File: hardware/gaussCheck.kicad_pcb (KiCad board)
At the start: 2 copper layers, 31.5 x 95.4 mm, 57 parts, among them J1 USB_C_Receptacle_USB2.0, J2 SWD, Q1 BSS138, Q2 BSS83P, SW1 PTS810, SW2 PT847S, SW3 PT847S, SW4 PT847S, U1 TLV493D, U2 VIM-878-DP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

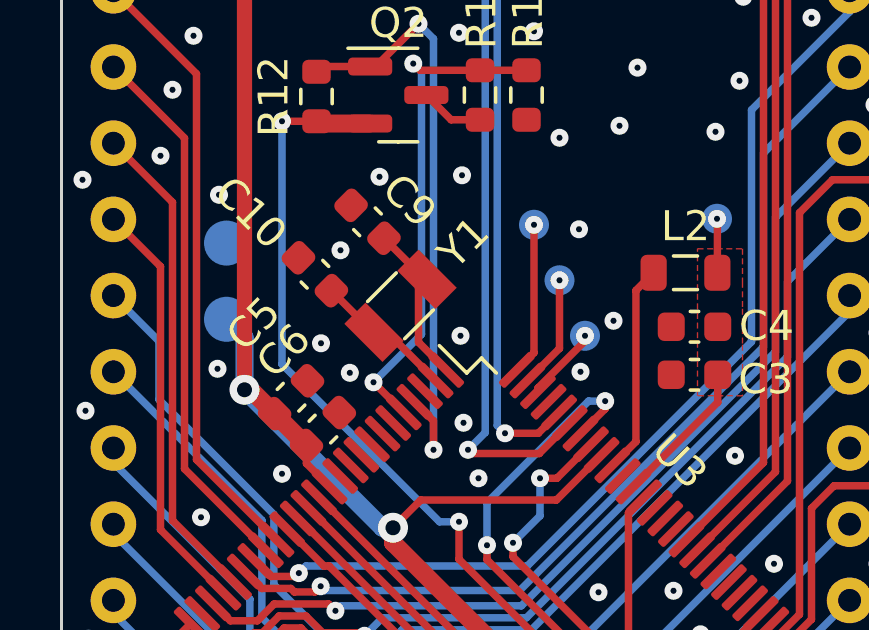
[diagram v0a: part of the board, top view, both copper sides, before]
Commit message: updated some MPNs
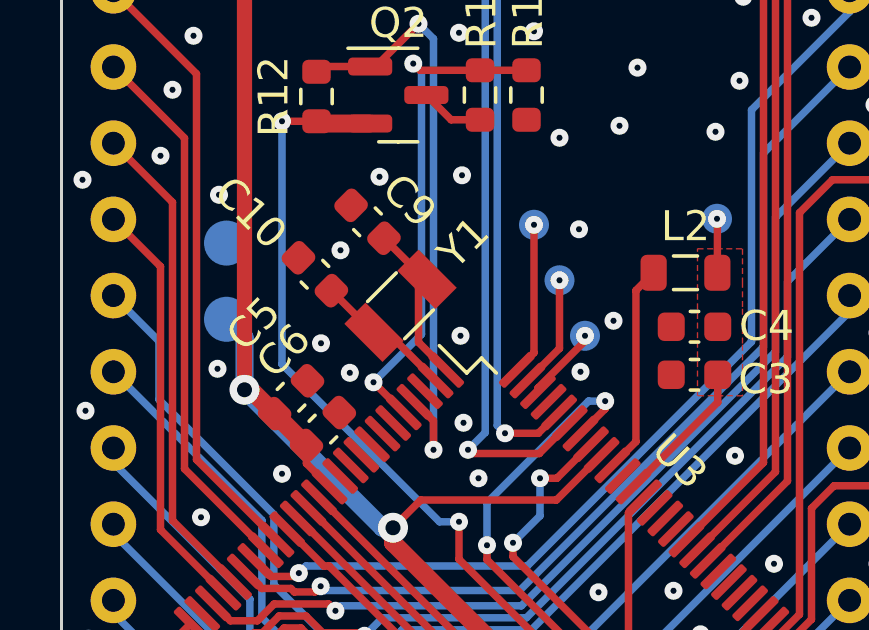
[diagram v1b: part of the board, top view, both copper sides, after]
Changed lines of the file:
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@@
   (segment (start 101.95 84.35) (end 101.95 85.6) (width 0.25) (layer "B.Cu") (net 46))
   (segment (start 105.324606 94.374606) (end 107.65 96.7) (width 0.25) (layer "B.Cu") (net 46))
-  (segment (start 97.9 79.232234) (end 97.9 78) (width 0.25) (layer "F.Cu") (net 47))
+  (segment (start 98.116117 77.716117) (end 96.748008 76.348008) (width 0.25) (layer "F.Cu") (net 47))
   (segment (start 98.824435 80.739154) (end 97.9 79.814719) (width 0.25) (layer "F.Cu") (net 47))
   (segment (start 98.183883 77.716117) (end 98.116117 77.716117) (width 0.25) (layer "F.Cu") (net 47))
-  (segment (start 97.9 79.814719) (end 97.9 79.3) (width 0.25) (layer "F.Cu") (net 47))
-  (segment (start 98.116117 77.716117) (end 96.748008 76.348008) (width 0.25) (layer "F.Cu") (net 47))
+  (segment (start 97.9 79.814719) (end 97.9 78) (width 0.25) (layer "F.Cu") (net 47))
   (segment (start 97.9 78) (end 98.183883 77.716117) (width 0.25) (layer "F.Cu") (net 47))
   (segment (start 96.862058 79.483883) (end 96.416117 79.483883) (width 0.25) (layer "F.Cu") (net 48))

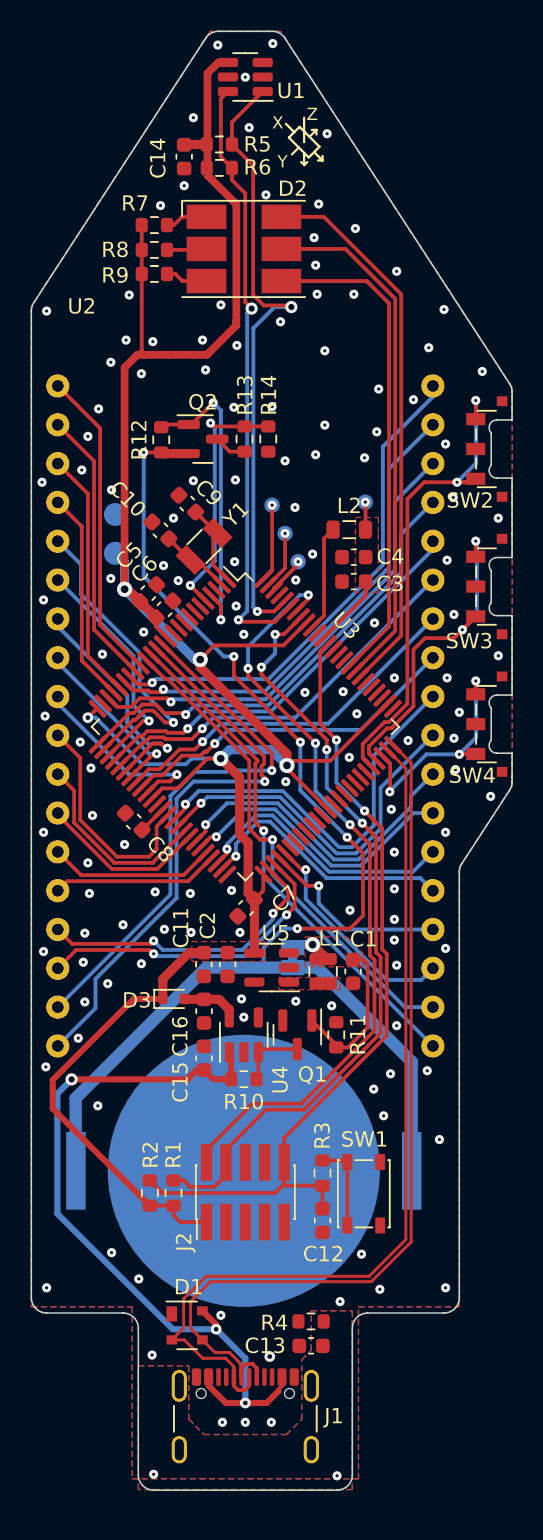
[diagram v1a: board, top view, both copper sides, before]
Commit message: added daughter board for LCD lightning
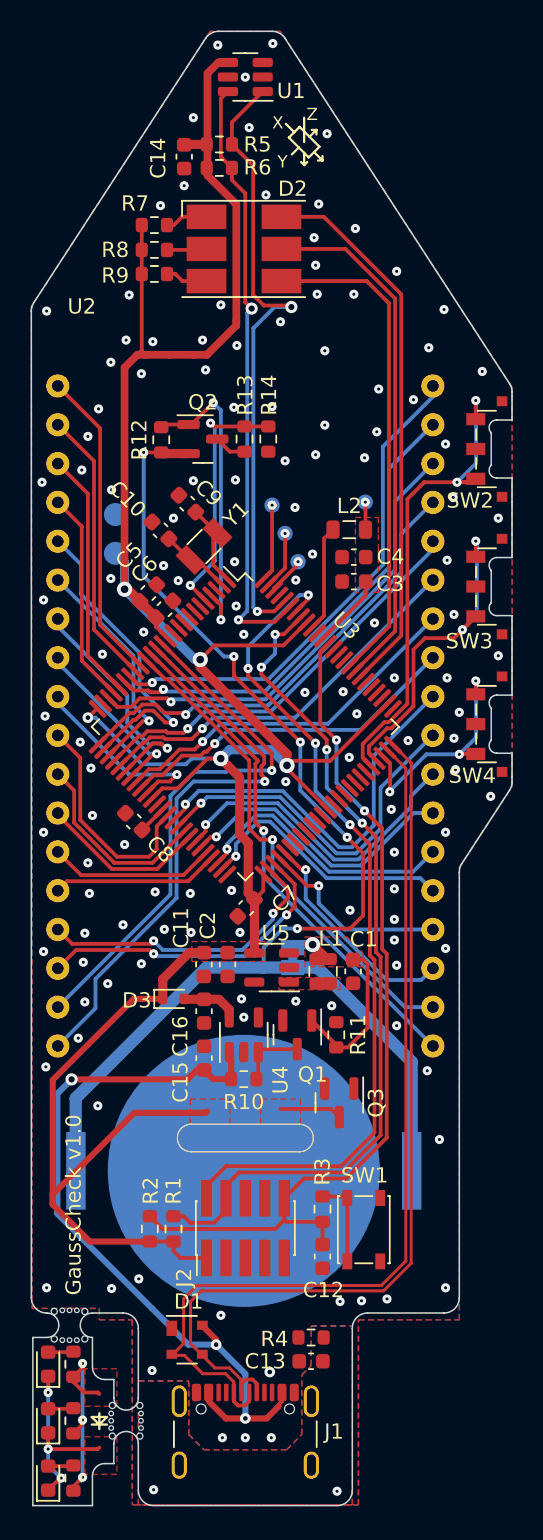
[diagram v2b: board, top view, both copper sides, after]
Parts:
- added D4: LED, LED_SMD:LED_0603_1608Metric, F.Cu at (87.1, 139.6)
- added D5: LED, LED_SMD:LED_0603_1608Metric, F.Cu at (87.1, 135.8)
- added D6: LED, LED_SMD:LED_0603_1608Metric, F.Cu at (87.1, 132.1)
- added Q3: BSS138, Package_TO_SOT_SMD:SOT-23, F.Cu at (106.2, 115.0)
- added R15: 140, Resistor_SMD:R_0603_1608Metric, F.Cu at (88.8, 139.6)
- added R16: 140, Resistor_SMD:R_0603_1608Metric, F.Cu at (88.8, 135.8)
- added R17: 140, Resistor_SMD:R_0603_1608Metric, F.Cu at (88.8, 132.1)
- added REF**: MouseBite_Mill1.6mm, GaussCheckCustomFootprint:MouseBite_Mill1.6mm, F.Cu at (92.2, 135.8)
- added REF**: MouseBite_Mill1.6mm, GaussCheckCustomFootprint:MouseBite_Mill1.6mm, F.Cu at (88.5, 129.6)
- C10, C9: value ??p -> 8p
- moved J2 2.35 mm to (100.0, 123.2)
- moved R3 2.35 mm to (105.0, 122.0)
- moved C12 2.35 mm to (105.0, 125.0)
- moved R1 2.35 mm to (95.3, 123.2)
- moved R2 2.35 mm to (93.8, 123.2)
- moved SW1 2.35 mm to (107.8, 123.3)
- moved R4 1.05 mm to (104.3, 130.3)
- moved C13 1.01 mm to (104.3, 131.9)
- moved J1 1.01 mm to (100.0, 137.6)
- moved D1 0.94 mm to (96.2, 130.5)
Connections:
- U3 pad 61: unconnected-(U3C-PC21/SLCD[41]-Pad61) -> /DisplayLightning/EN_DisplayLED
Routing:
- net +3V3: track 162.0 -> 179.7 mm
- net /DisplayLightning/LED_A: track 0.00 -> 13.2 mm, vias 0 -> 3
- net /DisplayLightning/LED_K: track 0.00 -> 12.6 mm, vias 0 -> 3
- net /MCU/SWDIO: track 50.4 -> 55.3 mm
- net /MCU/SWCLK: track 50.7 -> 55.6 mm
- net /DisplayLightning/D_LED_K: track 0.00 -> 4.07 mm
- net /MCU/~{RESET}: track 53.6 -> 57.5 mm
- net /MCU/D-: track 59.6 -> 61.4 mm
- net /MCU/D+: track 58.4 -> 60.2 mm
- net Net-(D6-A): track 0.00 -> 1.67 mm
- net Net-(D5-A): track 0.00 -> 1.67 mm
- net Net-(D4-A): track 0.00 -> 1.67 mm
- net GND: vias 135 -> 132
- added copper zone on F.Cu, net /DisplayLightning/D_LED_K
- added copper zone on F.Cu, net /DisplayLightning/LED_A
- added copper zone on F.Cu, net /DisplayLightning/LED_K
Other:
- board size 31.5 x 95.4 mm -> 31.5 x 96.4 mm
- board text added: "GaussCheck v1.0"

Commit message: custom LED daughter board for display lightning added resistors to USB-C CC line
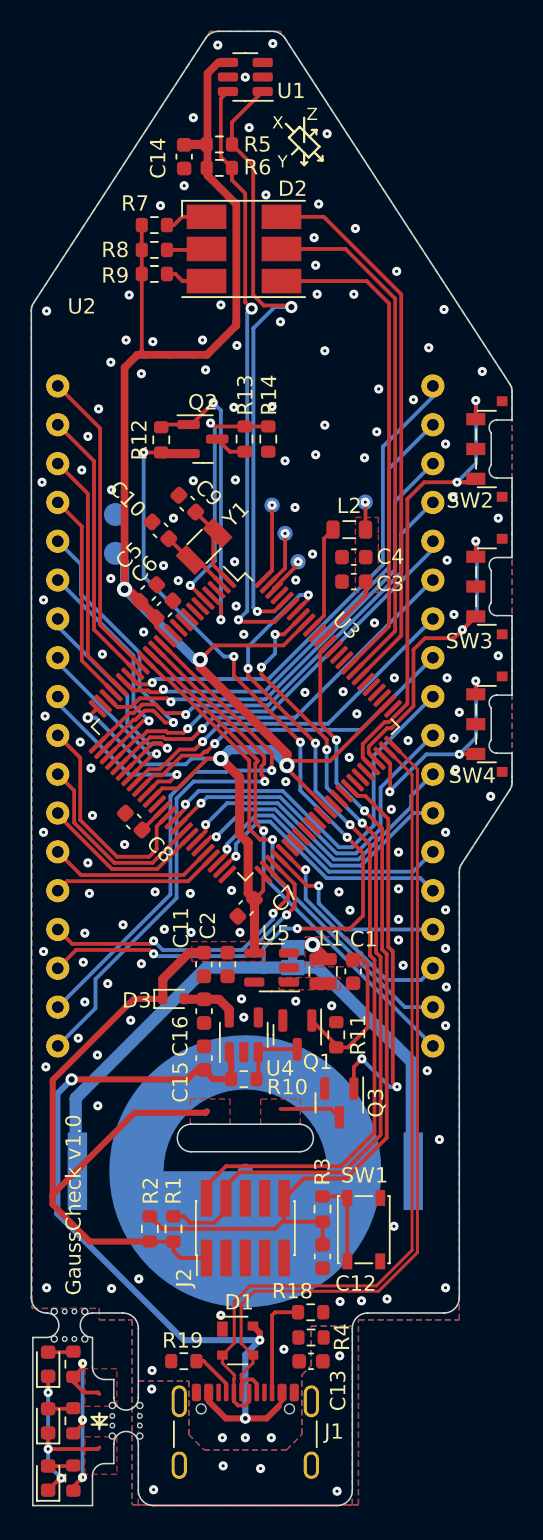
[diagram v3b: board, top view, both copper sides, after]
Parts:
- added R18: 56k, Resistor_SMD:R_0603_1608Metric, F.Cu at (104.3, 128.7)
- added R19: 56k, Resistor_SMD:R_0603_1608Metric, F.Cu at (96.0, 131.9)
- BT1: footprint Battery:BatteryHolder_Keystone_3034_1x20mm -> GaussCheckCustomFootprint:BatteryHolder_Keystone_3034_1x20mm_donut
- moved D1 3.31 mm to (99.5, 130.6)
- moved BT1 0.10 mm to (100.0, 119.5)
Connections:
- J1 pad A5: unconnected-(J1-CC1-PadA5) -> Net-(J1-CC1)
- J1 pad B5: unconnected-(J1-CC2-PadB5) -> Net-(J1-CC2)
- U3 pad 61: /DisplayLightning/EN_DisplayLED -> unconnected-(U3C-PC21/SLCD[41]-Pad61)
- U3 pad 67: unconnected-(U3B-PB19/SLCD[45]-Pad67) -> /DisplayLightning/EN_DisplayLED
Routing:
- net /DisplayLightning/EN_DisplayLED: track 0.00 -> 26.3 mm, vias 0 -> 2
- net Net-(J1-CC2): track 0.00 -> 6.83 mm
- net /MCU/D-: track 61.4 -> 55.4 mm
- net /MCU/D+: track 60.2 -> 55.6 mm
- net Net-(J1-CC1): track 0.00 -> 3.14 mm
- net VBUS: track 49.4 -> 51.6 mm
- net Net-(J1-SHIELD): vias 2 -> 6
- net GND: vias 132 -> 138

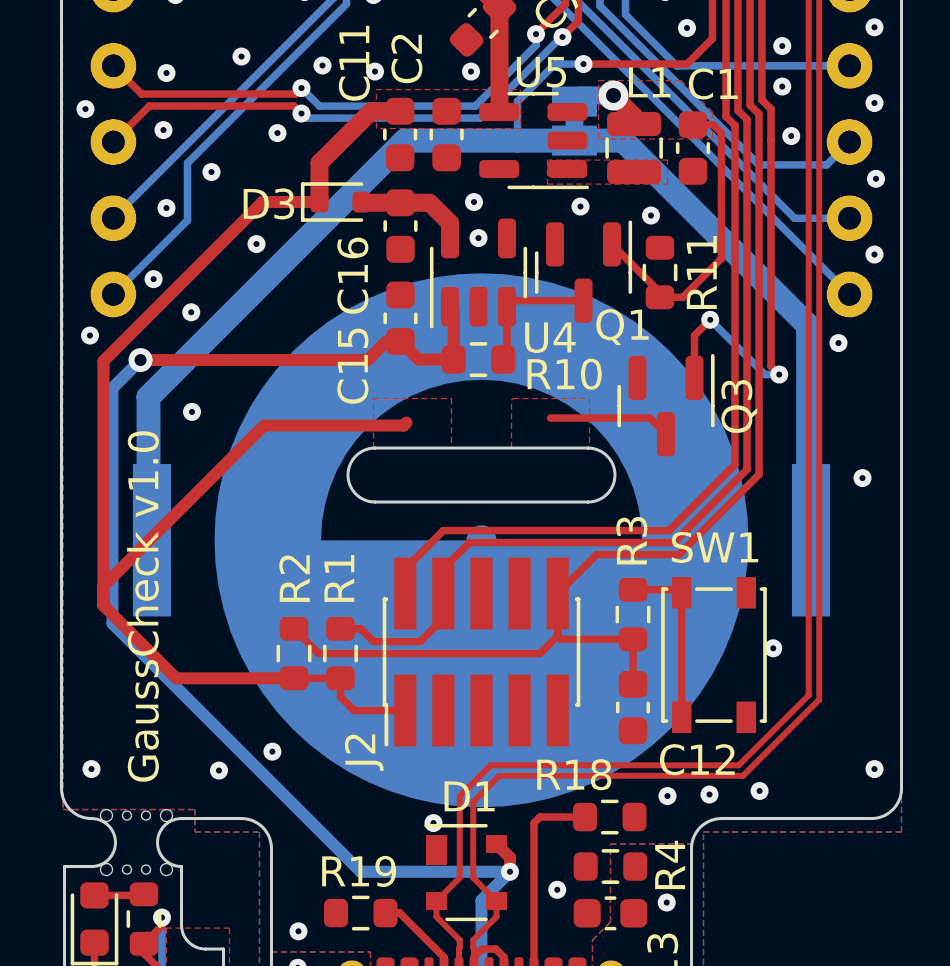
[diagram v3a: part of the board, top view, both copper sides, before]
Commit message: fixed battery footprint
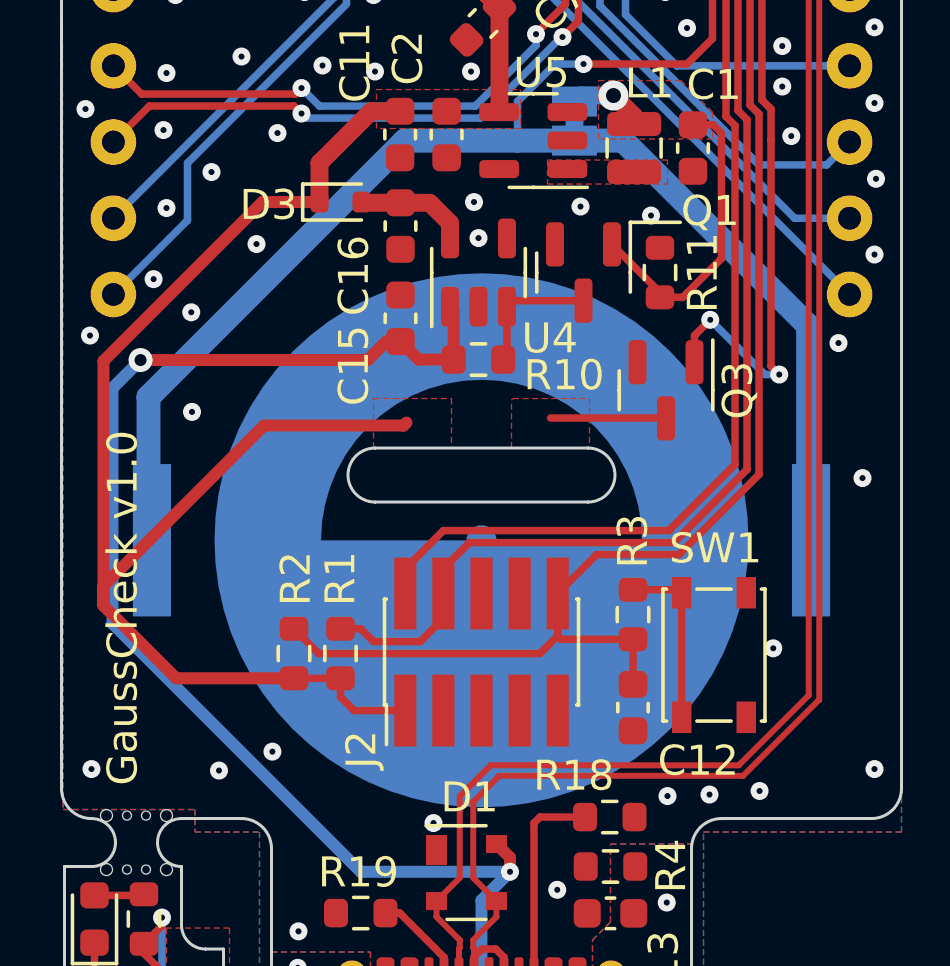
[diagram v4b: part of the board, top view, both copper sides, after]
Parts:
- moved Q3 0.53 mm to (106.2, 114.5)
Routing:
- net /DisplayLightning/EN_DisplayLED: track 26.3 -> 25.8 mm
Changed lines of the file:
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@@
   )
   (footprint "Package_TO_SOT_SMD:SOT-23" (layer "F.Cu")
-    (at 106.15 115 -90)
+    (at 106.15 114.475 -90)
     (descr "SOT, 3 Pin (https://www.jedec.org/system/files/docs/to-236h.pdf variant AB), generated with kicad-footprint-generator ipc_gullwing_generator.py")
     (tags "SOT TO_SOT_SMD")
@@
     (property "ki_keywords" "N-Channel MOSFET")
     (attr smd)
-    (fp_text reference "Q1" (at 1.775 -1.325 -180) (layer "F.SilkS")
+    (fp_text reference "Q1" (at -2.05 -4.225 -180) (layer "F.SilkS")
         (effects (font (size 1 1) (thickness 0.15)))
     )
@@
     (fp_arc (start 6 -8.55) (mid 7.90634 -8.911669) (end 9.325243 -7.588169)
       (stroke (width 0.12) (type solid)) (layer "B.SilkS"))
+    (fp_circle (center 0 0) (end 8.902486 0)
+      (stroke (width 0) (type solid)) (fill solid) (layer "B.Mask"))
     (fp_circle (center 0 0) (end 0 -10.25)
       (stroke (width 0.15) (type solid)) (fill none) (layer "Dwgs.User"))
@@
   (gr_line (start 89.95 135.55) (end 90.45 136.05)
     (stroke (width 0.15) (type default)) (layer "F.SilkS"))
+  (gr_line (start 104.96 108.875) (end 106.625 108.875)
+    (stroke (width 0.12) (type default)) (layer "F.SilkS"))
   (gr_line (start 104.2 51.8) (end 104.65 51.35)
     (stroke (width 0.15) (type default)) (layer "F.SilkS"))
@@
     (effects (font (size 0.8 0.8) (thickness 0.15)) (justify left bottom))
   )
-  (gr_text "GaussCheck v1.0" (at 89.35 127.6 90) (layer "F.SilkS" knockout)
+  (gr_text "GaussCheck v1.0" (at 88.625 127.65 90) (layer "F.SilkS" knockout)
     (effects (font (size 1 1) (thickness 0.15)) (justify left bottom))
   )
@@
   (segment (start 109.35 97.45) (end 109.35 104.8) (width 0.25) (layer "F.Cu") (net 109))
   (segment (start 109.35 104.8) (end 109.575 105.025) (width 0.25) (layer "F.Cu") (net 109))
-  (segment (start 107.625 112.125) (end 107.1 112.65) (width 0.25) (layer "F.Cu") (net 109))
   (segment (start 109.35 96.425) (end 109.35 97.45) (width 0.25) (layer "F.Cu") (net 109))
   (segment (start 109.65 105.1) (end 109.65 106.125) (width 0.25) (layer "F.Cu") (net 109))
   (segment (start 109.65 113.675) (end 109.925 113.95) (width 0.25) (layer "F.Cu") (net 109))
+  (segment (start 107.625 112.125) (end 107.1 112.65) (width 0.25) (layer "F.Cu") (net 109))
   (segment (start 108.425 95.5) (end 109.35 96.425) (width 0.25) (layer "F.Cu") (net 109))
-  (segment (start 107.1 112.65) (end 107.1 114.0625) (width 0.25) (layer "F.Cu") (net 109))
   (segment (start 107.351827 94.9234) (end 107.8484 94.9234) (width 0.25) (layer "F.Cu") (net 109))
+  (segment (start 107.1 112.65) (end 107.1 113.5375) (width 0.25) (layer "F.Cu") (net 109))
   (via (at 107.625 112.125) (size 0.6) (drill 0.2) (layers "F.Cu" "B.Cu") (net 109))
   (via (at 109.925 113.95) (size 0.6) (drill 0.2) (layers "F.Cu" "B.Cu") (net 109))
@@
   (segment (start 89.35 135.75) (end 89.35 132.05) (width 0.25) (layer "B.Cu") (net 111))
   (segment (start 89.35 139.5) (end 89.35 135.75) (width 0.25) (layer "B.Cu") (net 111))
-  (segment (start 106.15 115.9375) (end 105.6125 115.4) (width 0.25) (layer "F.Cu") (net 112))
-  (segment (start 105.6125 115.4) (end 102.3 115.4) (width 0.25) (layer "F.Cu") (net 112))
+  (segment (start 106.1375 115.4) (end 102.3 115.4) (width 0.25) (layer "F.Cu") (net 112))
+  (segment (start 106.15 115.4125) (end 106.1375 115.4) (width 0.25) (layer "F.Cu") (net 112))
   (segment (start 98.75 133.375001) (end 98.75 133.95) (width 0.25) (layer "F.Cu") (net 113))
   (segment (start 97.274999 131.9) (end 98.75 133.375001) (width 0.25) (layer "F.Cu") (net 113))
@@
     )
   )
-  (group "" (id faa8d76b-32d0-44ac-87b1-2593a7d4f948)
-    (members
-      283a6e0f-a399-4ad0-803d-3a6f3799cd7b
-      2b40e77f-f2be-4212-9ca3-20599938891c
-      3c184e25-103d-4fcc-88df-4fa1ac12720e
-      53e3d6ff-6081-4ed1-ba47-913a97d03e8a
-      58a7b288-5d4d-428b-a6fb-a8b97c33eb1e
-      682ab5db-4146-4898-9914-c75067c7605c
-      c02efa90-b71d-428f-8bd2-8f9990dd37a1
-    )
-  )
   (group "" (id e454f09e-1b85-4331-b996-6566700825e6)
     (members
@@
     )
   )
+  (group "" (id faa8d76b-32d0-44ac-87b1-2593a7d4f948)
+    (members
+      082b5c3d-1ffd-4ef5-9e65-d3a5d5bb26a8
+      283a6e0f-a399-4ad0-803d-3a6f3799cd7b
+      2b40e77f-f2be-4212-9ca3-20599938891c
+      3c184e25-103d-4fcc-88df-4fa1ac12720e
+      53e3d6ff-6081-4ed1-ba47-913a97d03e8a
+      58a7b288-5d4d-428b-a6fb-a8b97c33eb1e
+      682ab5db-4146-4898-9914-c75067c7605c
+      c02efa90-b71d-428f-8bd2-8f9990dd37a1
+    )
+  )
